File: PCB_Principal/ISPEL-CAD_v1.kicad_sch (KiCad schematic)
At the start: 27 parts, among them J1 Vin, J10 CN7_NUCLEO, J11 CN10_NUCLEO, J12 GND_NUCLEO, J13 E1, J14 S1, J15 E2, J16 S2, J17 FRENTE, J18 PRUEBA_5V, J2 V5, J3 VREG, J4 TEMP, J5 GND_NUCLEO, J6 CN8_NUCLEO, J7 CN9_NUCLEO, J8 GND_NUCLEO, J9 GND_NUCLEO

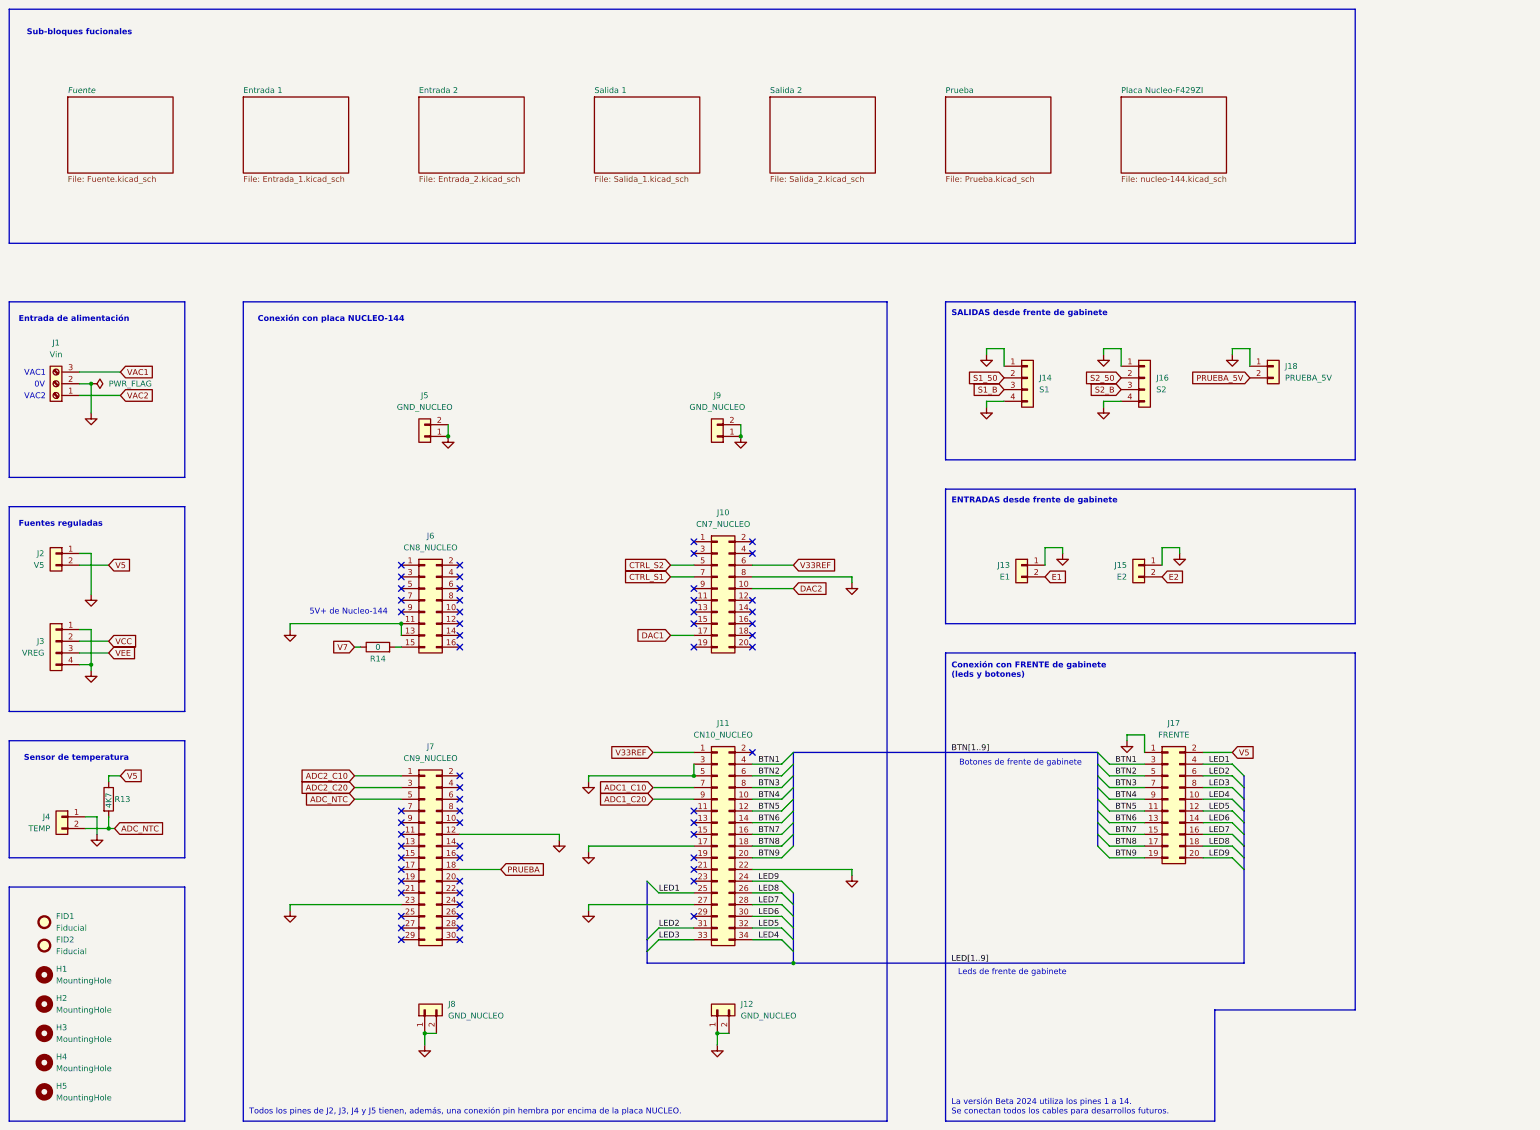
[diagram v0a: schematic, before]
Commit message: Agregado de zócalo +7V y pruebas.
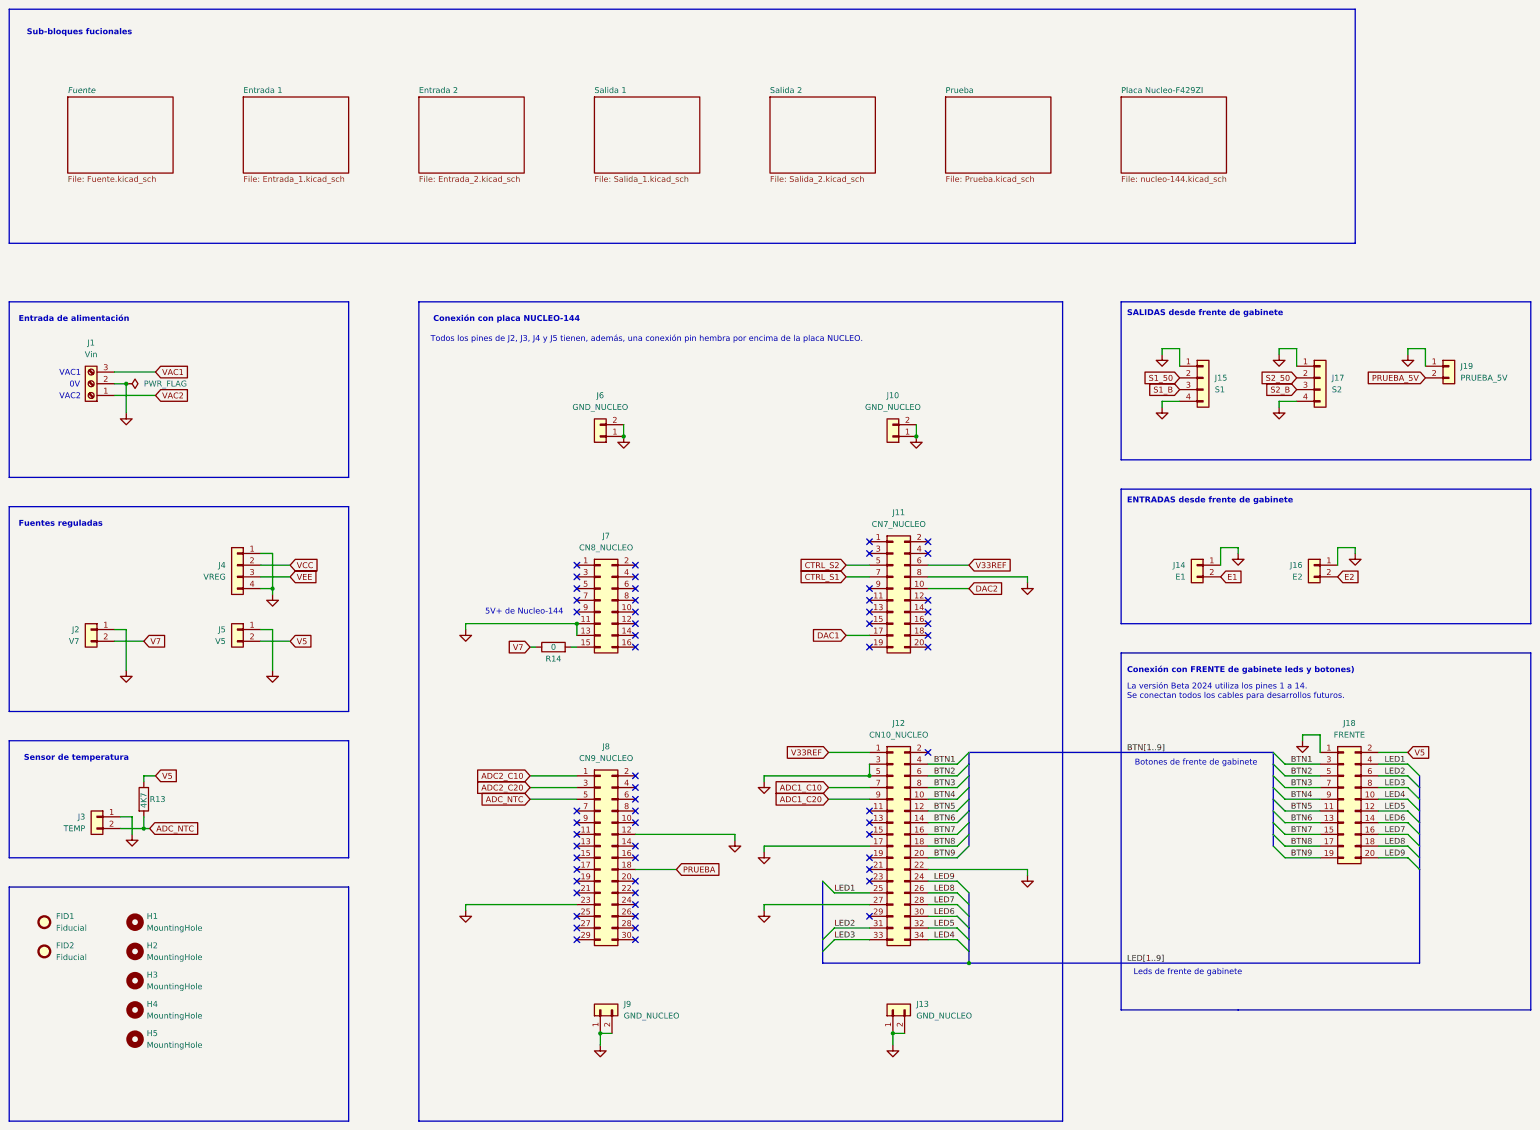
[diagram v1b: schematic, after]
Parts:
- added J2: V7, Connector_PinSocket_2.54mm:PinSocket_1x02_P2.54mm_Vertical, symbol Connector_Generic:Conn_01x02
- renumbered J9 to J10, J10 to J11, J11 to J12, J12 to J13, J13 to J14, J14 to J15, J15 to J16, J16 to J17, J17 to J18, J18 to J19, J4 to J3, J3 to J4, J2 to J5, J5 to J6, J6 to J7, J7 to J8, J8 to J9
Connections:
- net GND: now also J2.1 (Pin_1)
- net V7: now also J2.2 (Pin_2)
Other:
- note added: "Conexión con FRENTE de gabinete leds y botones)"
- note removed: "Conexión con FRENTE de gabinete (leds y botones)"
- moved on the sheet: FID2, H1, H2, H3, H4, H5, J1, J10, J11, J12, J13, J14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

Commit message: Versión 1 - ISPEL Beta 2024 para fabricar.
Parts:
- added R15: 1, Resistor_SMD:R_1206_3216Metric_Pad1.30x1.75mm_HandSolder, symbol Device:R
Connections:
- net V5: now also R15.2; no longer J18.2 (Pin_2)
- new net: J18.2 (Pin_2), R15.1
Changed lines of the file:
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@@
 	(wire
 		(pts
+			(xy 339.09 186.69) (xy 341.63 186.69)
+		)
+		(stroke
+			(width 0)
+			(type default)
+		)
+	)
+	(wire
+		(pts
 			(xy 302.26 189.23) (xy 309.88 189.23)
 		)
@@
 	(wire
 		(pts
-			(xy 328.93 186.69) (xy 322.58 186.69)
-		)
-		(stroke
-			(width 0)
-			(type default)
-		)
-	)
-	(wire
-		(pts
 			(xy 224.79 217.17) (xy 231.14 217.17)
 		)
@@
 		)
 	)
+	(wire
+		(pts
+			(xy 322.58 186.69) (xy 331.47 186.69)
+		)
+		(stroke
+			(width 0)
+			(type default)
+		)
+	)
 	(bus
 		(pts
@@
 	(global_label "V5"
 		(shape input)
-		(at 328.93 186.69 0)
+		(at 341.63 186.69 0)
 		(fields_autoplaced yes)
 		(effects
@@
 		)
 		(property "Intersheetrefs" "${INTERSHEET_REFS}"
-			(at 334.2133 186.69 0)
+			(at 346.9133 186.69 0)
 			(effects
 				(font
@@
 					(unit 1)
 				)
+			)
+		)
+	)
+	(symbol
+		(lib_id "Device:R")
+		(at 335.28 186.69 90)
+		(unit 1)
+		(exclude_from_sim no)
+		(in_bom yes)
+		(on_board yes)
+		(dnp no)
+		(property "Reference" "R15"
+			(at 337.058 184.15 90)
+			(effects
+				(font
+					(size 1.27 1.27)
+				)
+				(justify left)
+			)
+		)
+		(property "Value" "1"
+			(at 337.058 186.69 90)
+			(effects
+				(font
+					(size 1.27 1.27)
+				)
+				(justify left)
+			)
+		)
+		(property "Footprint" "Resistor_SMD:R_1206_3216Metric_Pad1.30x1.75mm_HandSolder"
+			(at 335.28 188.468 90)
+			(effects
+				(font
+					(size 1.27 1.27)
+				)
+				(hide yes)
+			)
+		)
+		(property "Datasheet" "~"
+			(at 335.28 186.69 0)
+			(effects
+				(font
+					(size 1.27 1.27)
+				)
+				(hide yes)
+			)
+		)
+		(property "Description" "Resistor"
+			(at 335.28 186.69 0)
+			(effects
+				(font
+					(size 1.27 1.27)
+				)
+				(hide yes)
+			)
+		)
+		(pin "2"
+		)
+		(pin "1"
+		)
+		(instances
+			(project "ISPEL-CAD_v1"
+				(path "/f66f0001-c0b9-4d2c-a26f-f2bac9dfd594"
+					(reference "R15")
+					(unit 1)
+				)

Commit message: Revisión 1. Con prototipo ISPEL Beta 2024 en fase de prueba.
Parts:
- R14: value 0 -> 0.1
- R15: value 1 -> 0.1
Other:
- removed sheet Placa Nucleo-F429ZI
- title: Placa principal ISPEL Beta 2024 -> Placa principal ISPEL Beta
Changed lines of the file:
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@@
 	(paper "A3")
 	(title_block
-		(title "Placa principal ISPEL Beta 2024")
-		(date "2024-10-30")
-		(rev "2 (GC)")
+		(title "Placa principal ISPEL Beta")
+		(date "2025-04-04")
+		(rev "1")
 		(company "Undav")
 	)
@@
 	(rectangle
 		(start 25.4 184.15)
-		(end 99.06 209.55)
+		(end 101.6 209.55)
 		(stroke
 			(width 0)
@@
 	(rectangle
 		(start 25.4 215.9)
-		(end 99.06 266.7)
+		(end 101.6 266.7)
 		(stroke
 			(width 0)
@@
 	(rectangle
 		(start 25.4 25.4)
-		(end 317.5 76.2)
+		(end 355.6 76.2)
 		(stroke
 			(width 0)
@@
 	(rectangle
 		(start 25.4 133.35)
-		(end 99.06 177.8)
+		(end 101.6 177.8)
 		(stroke
 			(width 0)
@@
 	(rectangle
 		(start 25.4 88.9)
-		(end 99.06 127)
+		(end 101.6 127)
 		(stroke
 			(width 0)
@@
 			)
 		)
-		(property "Value" "0"
+		(property "Value" "0.1"
 			(at 143.51 163.83 90)
 			(effects
@@
 			)
 		)
-		(property "Value" "1"
+		(property "Value" "0.1"
 			(at 337.058 186.69 90)
 			(effects
@@
 				)
 			)
-		)
-	)
-	(sheet
-		(at 266.7 44.45)
-		(size 22.86 16.51)
-		(fields_autoplaced yes)
-		(stroke
-			(width 0.1524)
-			(type solid)
-		)
-		(fill
-			(color 0 0 0 0.0000)
-		)
-		(property "Sheetname" "Placa Nucleo-F429ZI"
-			(at 266.7 43.7384 0)
-			(effects
-				(font
-					(size 1.27 1.27)
-				)
-				(justify left bottom)
-			)
-		)
-		(property "Sheetfile" "nucleo-144.kicad_sch"
-			(at 266.7 61.5446 0)
-			(effects
-				(font
-					(size 1.27 1.27)
-				)
-				(justify left top)
-			)
-		)
-		(instances
-			(project "ISPEL-CAD_v1"
-				(path "/f66f0001-c0b9-4d2c-a26f-f2bac9dfd594"
-					(page "8")
-				)
-			)
